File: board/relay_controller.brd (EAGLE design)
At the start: 70 x 50 mm, 55 parts, among them IC1 STM32F103C8T, IC3 AT24C, X1 RJ45-8L21-S, X2 RJ45-8L21-S

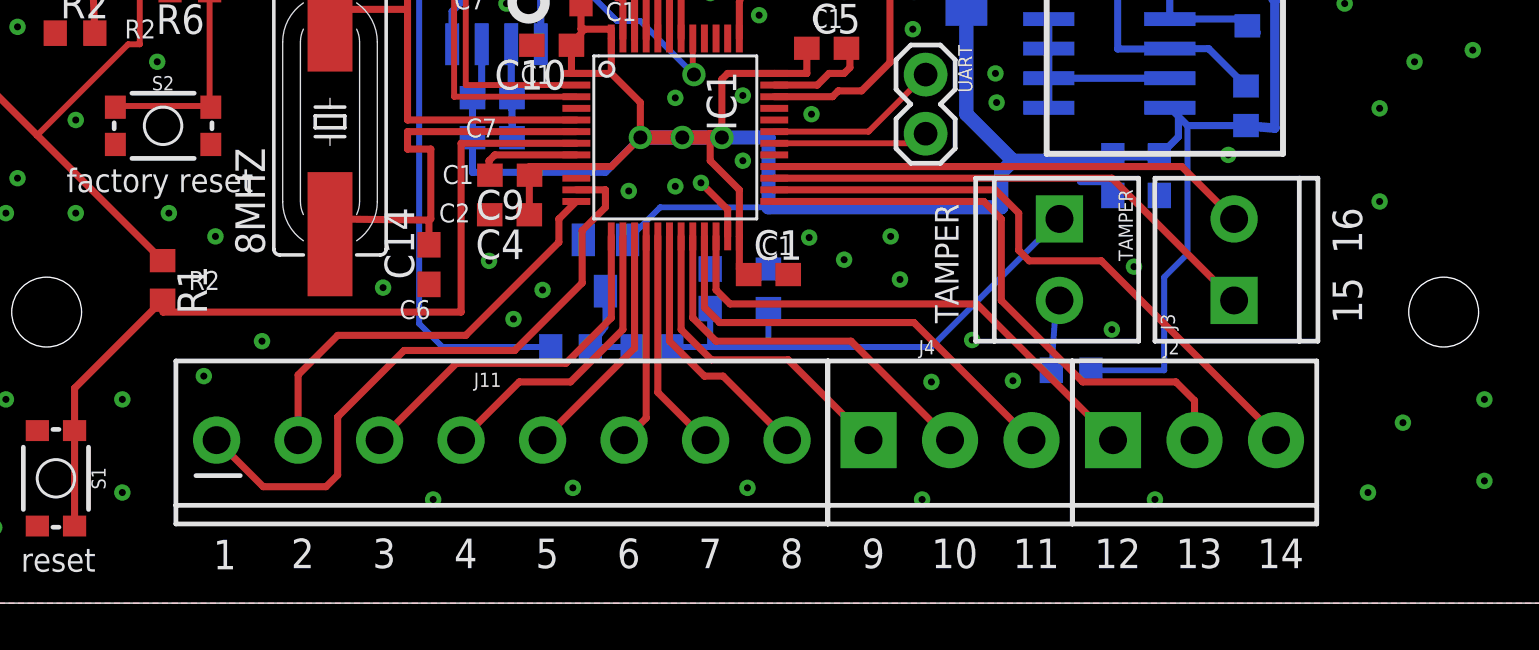
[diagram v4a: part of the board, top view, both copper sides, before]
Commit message: add current limiting resistor
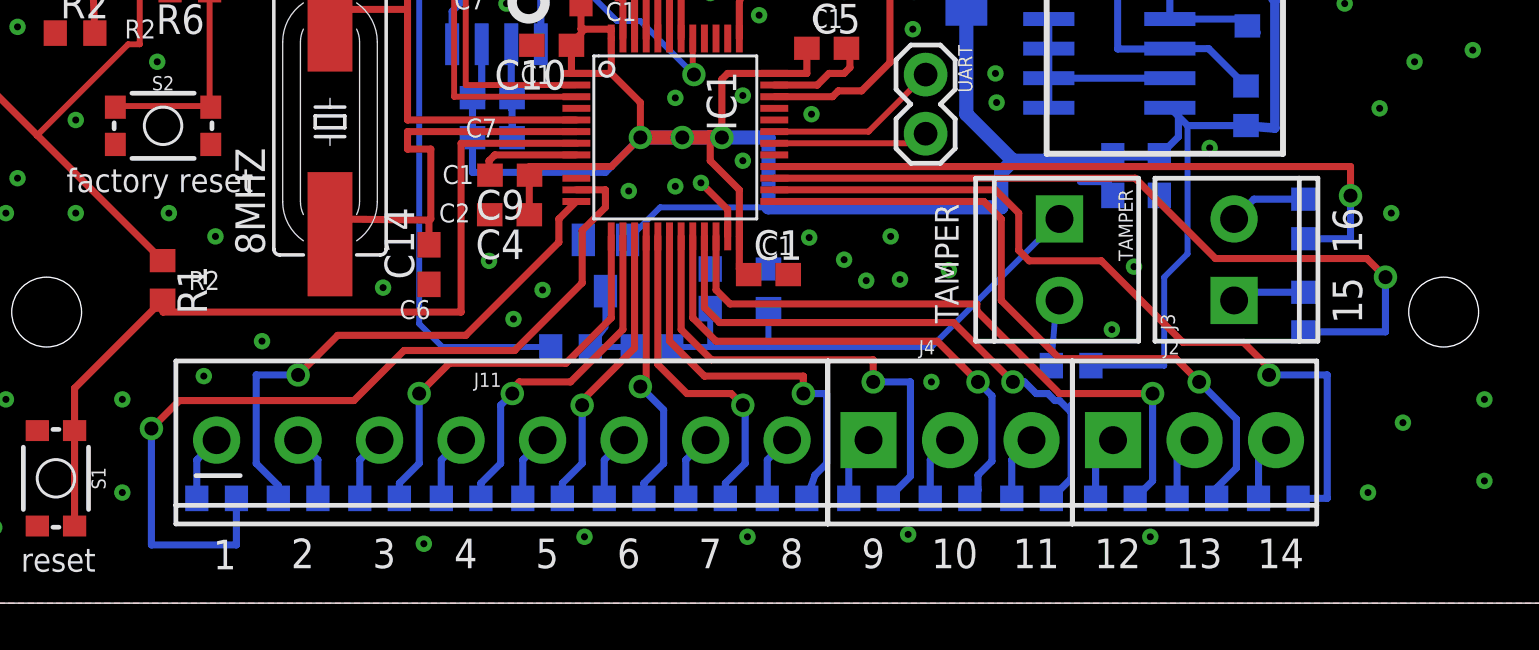
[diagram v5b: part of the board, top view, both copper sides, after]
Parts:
- added R10, R11, R12, R13, R14, R15, R16, R17, R18, R19, R20, R21, R22, R23, R8, R9: (no value), resistor:R0603
- moved R60 0.20 mm to (49.0, 10.2)
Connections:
- new net N$13: J2.3, R10.1
- new net N$14: J2.2, R11.1
- new net N$15: J2.1, R12.1
- new net N$16: J4.3, R13.1
- new net N$18: J4.2, R14.1
- new net N$19: J4.1, R15.1
- new net N$21: J11.8, R16.1
- new net N$22: J11.7, R17.1
- new net N$23: J11.6, R18.1
- new net N$24: J11.5, R19.1
- new net N$25: J11.1, R20.1
- new net N$26: J11.2, R21.1
- new net N$27: J11.4, R22.1
- new net N$28: J11.3, R23.1
- new net N$4: J3.2, R8.1
- new net N$9: J3.1, R9.1
- net RELAY_1: now also R20.2; no longer J11.1
- net RELAY_10: now also R14.2; no longer J4.2
- net RELAY_11: now also R13.2; no longer J4.3
- net RELAY_12: now also R12.2; no longer J2.1
- net RELAY_13: now also R11.2; no longer J2.2
- net RELAY_14: now also R10.2; no longer J2.3
- net RELAY_15: now also R9.2; no longer J3.1
- net RELAY_16: now also R8.2; no longer J3.2
- net RELAY_2: now also R21.2; no longer J11.2
- net RELAY_3: now also R23.2; no longer J11.3
- net RELAY_4: now also R22.2; no longer J11.4
- net RELAY_5: now also R19.2; no longer J11.5
- net RELAY_6: now also R18.2; no longer J11.6
- net RELAY_7: now also R17.2; no longer J11.7
- net RELAY_8: now also R16.2; no longer J11.8
- net RELAY_9: now also R15.2; no longer J4.1
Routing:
- net RELAY_15: track 21.9 -> 33.9 mm, vias 0 -> 1
- net RELAY_1: track 27.3 -> 37.4 mm, vias 0 -> 1
- net RELAY_16: track 20.7 -> 29.9 mm, vias 0 -> 1
- net RELAY_14: track 27.1 -> 34.7 mm, vias 0 -> 1
- net RELAY_9: track 14.0 -> 20.7 mm, vias 0 -> 1
- net RELAY_8: track 11.3 -> 17.4 mm, vias 0 -> 1
- net RELAY_12: track 22.0 -> 27.9 mm, vias 0 -> 1
- net RELAY_10: track 16.7 -> 22.5 mm, vias 0 -> 1
- net RELAY_11: track 19.5 -> 25.0 mm, vias 0 -> 1
- net RELAY_2: track 18.4 -> 23.1 mm, vias 0 -> 1
- net RELAY_7: track 9.60 -> 14.3 mm, vias 0 -> 1
- net RELAY_13: track 25.3 -> 29.5 mm, vias 0 -> 1
- net N$4: track 0.00 -> 3.35 mm
- net RELAY_6: track 9.14 -> 12.4 mm, vias 0 -> 1
- net N$9: track 0.00 -> 3.14 mm
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
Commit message: refresh libs
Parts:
- removed U$2, U$3: (no value), mounting:DIN-MOUNT-2-HOLE
- added U$4, U$5: (no value), mounting:C45-DIN-MOUNT-2-HOLE
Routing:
- net CAN_L: track 47.6 -> 50.4 mm
- net RELAY_15: track 33.9 -> 32.1 mm
- net +3V3: track 255.5 -> 257.0 mm
- net CAN_H: track 54.1 -> 53.2 mm
- net PRE_FUSE_12V: track 61.5 -> 62.3 mm
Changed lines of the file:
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@@
 <text x="39" y="30.5" size="0.7" layer="121" rot="R90">GND</text>
 <text x="41.5" y="30.5" size="0.7" layer="121" rot="R90">swdio</text>
-<text x="3.85" y="39.35" size="0.8128" layer="121">R5</text>
-<text x="6.45" y="39.3" size="0.8128" layer="121">R5</text>
+<text x="1.85" y="40.35" size="0.8128" layer="121">R5</text>
+<text x="7.95" y="40.8" size="0.8128" layer="121">R5</text>
 <text x="1.5" y="48" size="0.8128" layer="122" rot="MR180">SHIELD</text>
 <text x="20.5" y="29.5" size="0.8128" layer="121">C6</text>
@@
 <element name="R4" library="rcl" package="R0603" value="1K" x="7" y="42" rot="R90"/>
 <element name="U$1" library="components" package="HW-613" value="HW-613" x="53" y="29.5" rot="R270"/>
-<element name="U$2" library="mounting" package="DIN-MOUNT-2-HOLE" value="" x="5" y="25"/>
-<element name="U$3" library="mounting" package="DIN-MOUNT-2-HOLE" value="" x="65" y="25"/>
 <element name="J11" library="SparkFun-Connectors" package="SCREWTERMINAL-3.5MM-8" value="" x="12.3" y="7"/>
 <element name="J2" library="SparkFun-Connectors" package="SCREWTERMINAL-3.5MM-3" value="" x="50.8" y="7">
@@
 <element name="R22" library="resistor" package="R0603" value="" x="22.8" y="4.5" rot="MR180"/>
 <element name="R23" library="resistor" package="R0603" value="" x="19.3" y="4.5" rot="MR180"/>
+<element name="U$4" library="mounting" package="C45-DIN-MOUNT-2-HOLE" value="" x="65" y="25"/>
+<element name="U$5" library="mounting" package="C45-DIN-MOUNT-2-HOLE" value="" x="5" y="25"/>
 </elements>
 <signals>
@@
 <via x="12.25" y="15.75" extent="1-16" drill="0.3"/>
 <via x="8.25" y="35.75" extent="1-16" drill="0.3"/>
-<via x="6.4" y="35.1" extent="1-16" drill="0.3"/>
+<via x="12.4" y="37.6" extent="1-16" drill="0.3"/>
 <via x="10.2" y="46.6" extent="1-16" drill="0.3"/>
 <via x="10.75" y="45.25" extent="1-16" drill="0.3"/>
@@
 <wire x1="23.685" y1="23.5" x2="23.685" y2="24.0025" width="0.4064" layer="16"/>
 <contactref element="LED1" pad="A"/>
-<wire x1="2" y1="33.55" x2="2" y2="47" width="0.6096" layer="1"/>
-<wire x1="2" y1="47" x2="4.5" y2="47" width="0.6096" layer="1"/>
+<wire x1="1.5" y1="33.55" x2="1.5" y2="47" width="0.6096" layer="1"/>
+<wire x1="1.5" y1="47" x2="4.5" y2="47" width="0.6096" layer="1"/>
 <wire x1="4.5" y1="47" x2="4.5" y2="47.05" width="0.6096" layer="1"/>
-<wire x1="2" y1="33.55" x2="4.01" y2="33.55" width="0.254" layer="1"/>
+<wire x1="1.5" y1="33.55" x2="4.01" y2="33.55" width="0.254" layer="1"/>
 <wire x1="4.01" y1="33.55" x2="4.01" y2="30.5" width="0.254" layer="1"/>
-<wire x1="2" y1="33.55" x2="2" y2="22.69" width="0.3048" layer="1"/>
+<wire x1="1.5" y1="33.55" x2="2" y2="22.69" width="0.3048" layer="1"/>
 <wire x1="2" y1="22.69" x2="4.595" y2="20.095" width="0.3048" layer="1"/>
 <wire x1="4.595" y1="20.095" x2="9.98" y2="14.71" width="0.3048" layer="1"/>
@@
 <wire x1="34.75" y1="17.75" x2="33.5" y2="19" width="0.3048" layer="1"/>
 <wire x1="33.5" y1="19" x2="33.5" y2="20" width="0.3048" layer="1"/>
-<wire x1="2" y1="33.55" x2="47" y2="33.55" width="0.6096" layer="1"/>
+<wire x1="1.5" y1="33.55" x2="47" y2="33.55" width="0.6096" layer="1"/>
 <contactref element="F1" pad="2"/>
 <wire x1="47" y1="33.55" x2="47" y2="29" width="0.6096" layer="1"/>
@@
 <wire x1="10" y1="12.5" x2="10" y2="13.01" width="0.3048" layer="1"/>
 <wire x1="10" y1="13.01" x2="9.98" y2="13.01" width="0.3048" layer="1"/>
-<wire x1="6.2" y1="7.41" x2="6.2" y2="9.23" width="0.3048" layer="1"/>
-<wire x1="6.2" y1="9.23" x2="9.98" y2="13.01" width="0.3048" layer="1"/>
+<wire x1="6.2" y1="7.41" x2="6.2" y2="8.23" width="0.3048" layer="1"/>
+<wire x1="6.2" y1="8.23" x2="9.98" y2="13.01" width="0.3048" layer="1"/>
 <wire x1="6.2" y1="3.31" x2="6.2" y2="7.41" width="0.3048" layer="1"/>
 </signal>
@@
 <wire x1="45.75" y1="31.35519375" x2="45.75" y2="34.68" width="0.3048" layer="16"/>
 <wire x1="45.75" y1="34.68" x2="46" y2="34.93" width="0.3048" layer="16"/>
-<wire x1="46" y1="34.93" x2="46" y2="39" width="0.3048" layer="16"/>
-<wire x1="46" y1="39" x2="42.795" y2="39" width="0.3048" layer="16"/>
-<wire x1="42.795" y1="39" x2="41.945" y2="38.15" width="0.3048" layer="16" curve="90"/>
+<wire x1="46" y1="34.93" x2="46" y2="35" width="0.3048" layer="16"/>
 <wire x1="45.75" y1="31.35519375" x2="45.44480625" y2="31.05" width="0.3048" layer="16"/>
 <wire x1="45.44480625" y1="31.05" x2="35.2" y2="31.05" width="0.3048" layer="16"/>
@@
 <wire x1="24.955" y1="32" x2="34.25" y2="32" width="0.3048" layer="16"/>
 <wire x1="34.25" y1="32" x2="35.2" y2="31.05" width="0.3048" layer="16"/>
-<wire x1="25.495" y1="38.18" x2="25.495" y2="38.495" width="0.3048" layer="16"/>
-<wire x1="25.495" y1="38.495" x2="27.5" y2="40" width="0.3048" layer="16"/>
-<wire x1="27.5" y1="40" x2="40.5" y2="40" width="0.3048" layer="16"/>
-<wire x1="40.5" y1="40" x2="41.5" y2="39.5" width="0.3048" layer="16"/>
-<wire x1="41.5" y1="39.5" x2="41.5" y2="38.595" width="0.3048" layer="16"/>
-<wire x1="41.5" y1="38.595" x2="41.945" y2="38.15" width="0.3048" layer="16"/>
+<wire x1="25.495" y1="38.18" x2="26.815" y2="39.5" width="0.3048" layer="16"/>
+<wire x1="26.815" y1="39.5" x2="41.945" y2="39.5" width="0.3048" layer="16"/>
+<wire x1="41.945" y1="39.5" x2="41.945" y2="38.15" width="0.3048" layer="16"/>
+<wire x1="41.945" y1="39.5" x2="44" y2="39.5" width="0.3048" layer="16"/>
+<wire x1="44" y1="39.5" x2="45.75" y2="37.75" width="0.3048" layer="16"/>
+<wire x1="45.75" y1="37.75" x2="45.75" y2="34.68" width="0.3048" layer="16"/>
 </signal>
 <signal name="CAN_L">
@@
 <contactref element="D5" pad="1"/>
 <wire x1="23.685" y1="29.8375" x2="23.685" y2="31.3" width="0.3048" layer="16"/>
-<wire x1="43.85" y1="34.68" x2="43.85" y2="33.35393125" width="0.3048" layer="16"/>
 <contactref element="X2" pad="2"/>
 <wire x1="43.85" y1="34.68" x2="42.92" y2="35.61" width="0.3048" layer="16"/>
 <wire x1="42.92" y1="35.61" x2="40.675" y2="35.61" width="0.3048" layer="16"/>
-<wire x1="43.85" y1="33.35393125" x2="23.685" y2="33.35393125" width="0.3048" layer="16"/>
-<wire x1="23.685" y1="33.35393125" x2="23.685" y2="29.8375" width="0.3048" layer="16"/>
-<wire x1="40.675" y1="35.61" x2="40.675" y2="35.825" width="0.3048" layer="16"/>
-<wire x1="40.675" y1="35.825" x2="39.55" y2="36.9" width="0.3048" layer="16"/>
-<wire x1="39.55" y1="36.9" x2="25.635" y2="36.9" width="0.3048" layer="16"/>
-<wire x1="25.635" y1="36.9" x2="24.225" y2="35.64" width="0.3048" layer="16"/>
+<wire x1="43" y1="32.85393125" x2="23.685" y2="32.85393125" width="0.3048" layer="16"/>
+<wire x1="23.685" y1="32.85393125" x2="23.685" y2="29.8375" width="0.3048" layer="16"/>
+<wire x1="24.225" y1="35.64" x2="25.965" y2="33.9" width="0.3048" layer="16"/>
+<wire x1="25.965" y1="33.9" x2="42.9" y2="33.9" width="0.3048" layer="16"/>
+<wire x1="42.9" y1="33.9" x2="43.5" y2="34.5" width="0.3048" layer="16"/>
+<wire x1="43.5" y1="34.5" x2="44" y2="34.5" width="0.3048" layer="16"/>
+<wire x1="44" y1="34.5" x2="44" y2="33.85393125" width="0.3048" layer="16"/>
+<wire x1="44" y1="33.85393125" x2="43" y2="32.85393125" width="0.3048" layer="16"/>
+<wire x1="43.85" y1="34.68" x2="44" y2="34.53" width="0.3048" layer="16"/>
+<wire x1="44" y1="34.53" x2="44" y2="34.5" width="0.3048" layer="16"/>
 </signal>
 <signal name="N$17">
@@
 <contactref element="R9" pad="2"/>
 <wire x1="51.75" y1="18.25" x2="55.2" y2="14.8" width="0.3048" layer="1"/>
-<wire x1="55.2" y1="14.8" x2="61.7" y2="14.8" width="0.3048" layer="1"/>
-<wire x1="61.7" y1="14.8" x2="62.5" y2="14" width="0.3048" layer="1"/>
-<via x="62.5" y="14" extent="1-16" drill="0.6"/>
-<wire x1="62.5" y1="14" x2="62.5" y2="11.65" width="0.3048" layer="16"/>
-<wire x1="62.5" y1="11.65" x2="59" y2="11.65" width="0.3048" layer="16"/>
+<wire x1="55.2" y1="14.8" x2="61.2" y2="14.8" width="0.3048" layer="1"/>
+<wire x1="61.2" y1="14.8" x2="61.5" y2="14" width="0.3048" layer="1"/>
+<via x="61.5" y="14" extent="1-16" drill="0.6"/>
+<wire x1="61.5" y1="14" x2="61.5" y2="11.65" width="0.3048" layer="16"/>
+<wire x1="61.5" y1="11.65" x2="59" y2="11.65" width="0.3048" layer="16"/>
 </signal>
 <signal name="N$3">
@@
 <wire x1="56" y1="48" x2="54.5" y2="46.5" width="0.6096" layer="1"/>
 <wire x1="54.5" y1="46.5" x2="54.5" y2="44.5" width="0.6096" layer="1"/>
-<wire x1="14" y1="41.5" x2="54.5" y2="41.5" width="1.4224" layer="16"/>
-<wire x1="54.5" y1="41.5" x2="54.5" y2="44.5" width="1.4224" layer="16"/>
-<wire x1="14" y1="41.5" x2="12.73" y2="42.77" width="1.4224" layer="16"/>
-<wire x1="12.73" y1="42.77" x2="10.5" y2="42.77" width="1.4224" layer="16"/>
+<wire x1="13.4" y1="41" x2="54.2" y2="41" width="1.4224" layer="16"/>
+<wire x1="54.2" y1="41" x2="54.5" y2="44.5" width="1.4224" layer="16"/>
+<wire x1="13.4" y1="41" x2="12.43" y2="42.77" width="1.4224" layer="16"/>
+<wire x1="12.43" y1="42.77" x2="10.5" y2="42.77" width="1.4224" layer="16"/>
 </signal>
 <signal name="N$4">

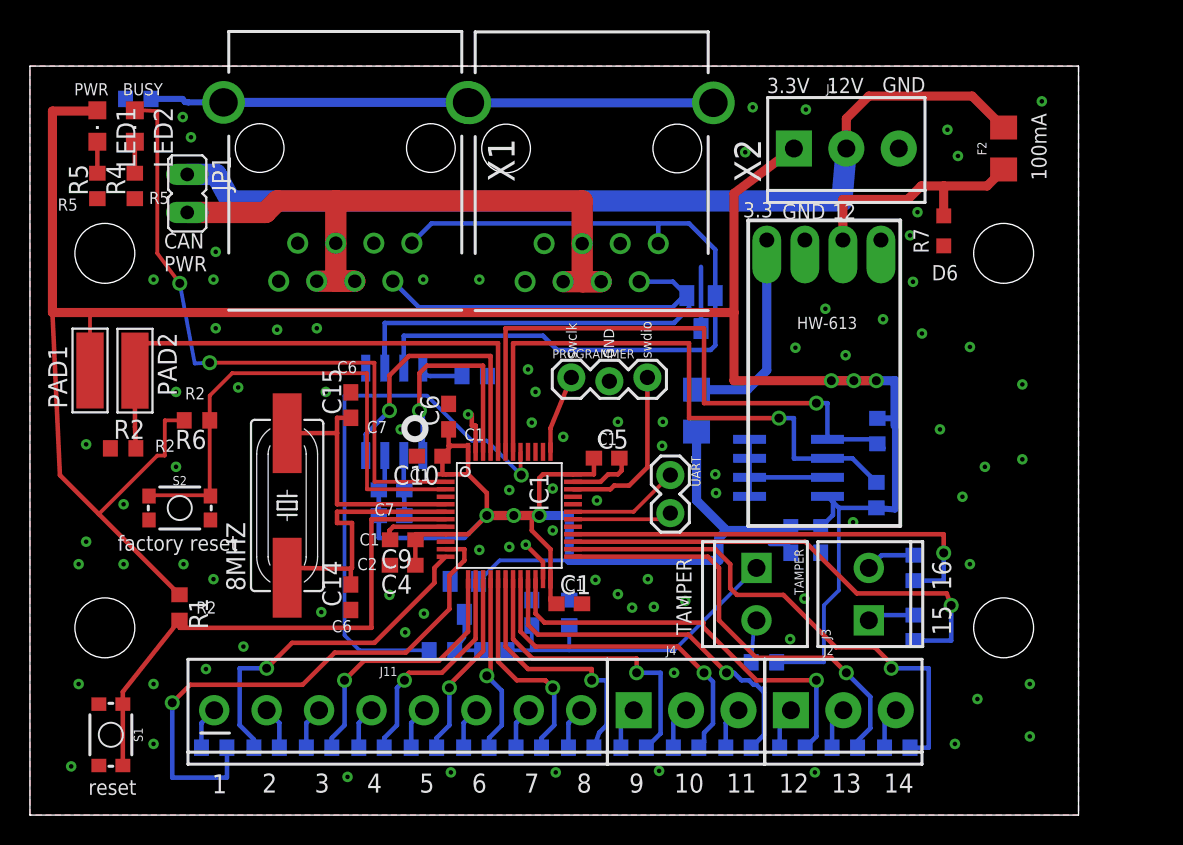
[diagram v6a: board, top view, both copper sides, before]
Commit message: increase size for 5mm inputs
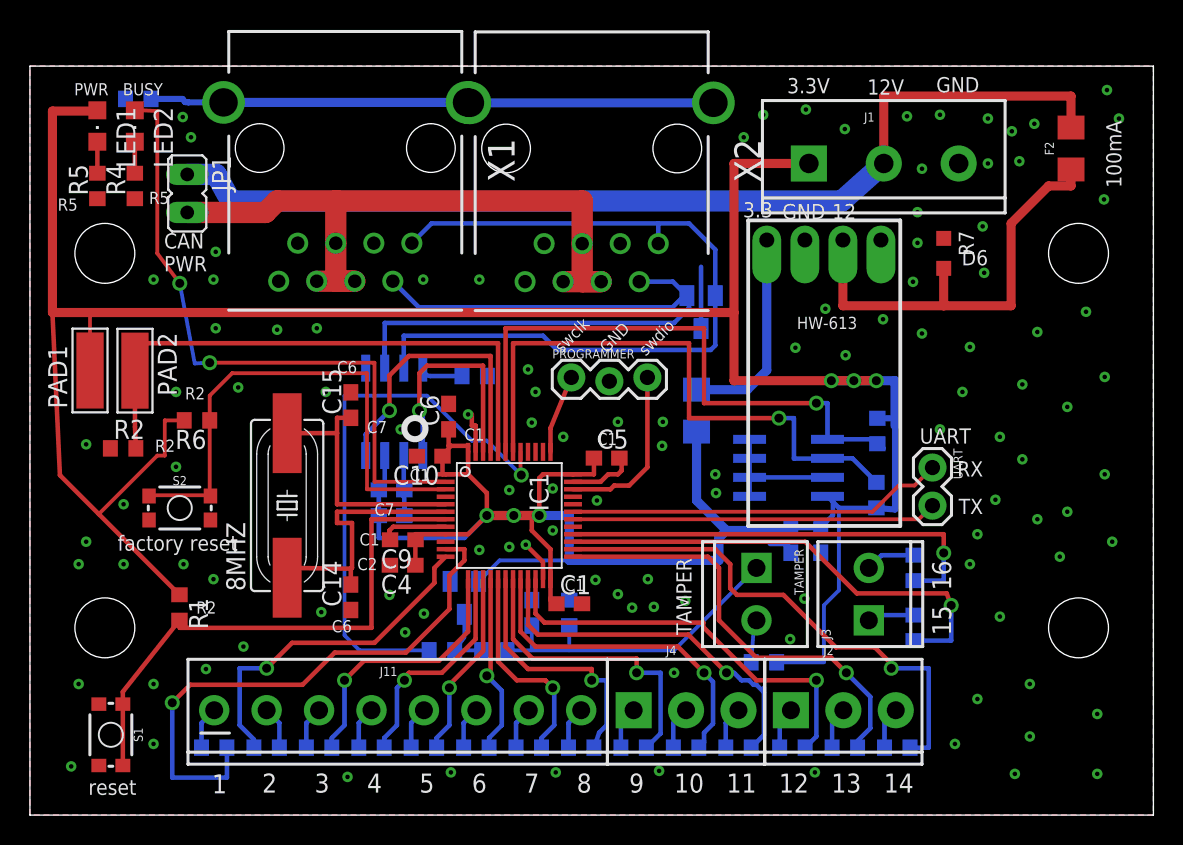
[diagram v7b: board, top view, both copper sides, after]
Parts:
- J1: device SparkFun-Connectors:SCREWTERMINAL-3.5MM-3 -> SparkFun-Connectors:SCREWTERMINAL-5MM-3
- moved UART 17.5 mm to (60.2, 23.2)
- moved U$4 5.00 mm to (70.0, 25.0)
- moved F2 4.50 mm to (69.5, 44.5)
- moved R7 1.50 mm to (61.0, 37.5), turned to 270 degrees
- moved J1 1.41 mm to (52.0, 43.5)
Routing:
- net UART_TX: track 6.67 -> 24.4 mm
- net UART_RX: track 7.51 -> 25.2 mm
- net +12V: track 16.3 -> 29.8 mm
- net PRE_FUSE_12V: track 62.3 -> 67.6 mm
- net +3V3: track 257.0 -> 259.0 mm
- net GND: vias 89 -> 114
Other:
- board size 70 x 50 mm -> 75 x 50 mm
- board text added: "RX"
- board text added: "TX"
- board text added: "UART"
- board text added: "relay controller 2020.07.13 v1.1"
- board text removed: "relay controller 2020.06.12 v1.1"
